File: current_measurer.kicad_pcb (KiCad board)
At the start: 2 copper layers, 104.9 x 128.5 mm, 31 parts, among them J1 Eurorack Power Input, J2 Eurorack Power Output, J3 Back_Conn_2, J4 Front_Conn_2, J5 Back_Conn_3, J6 Front_Conn_3, J7 Back_Conn_1, J8 Front_Conn_1, M2 MountingHole_2.2mm_M2, M3 MountingHole_3.2mm_M3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

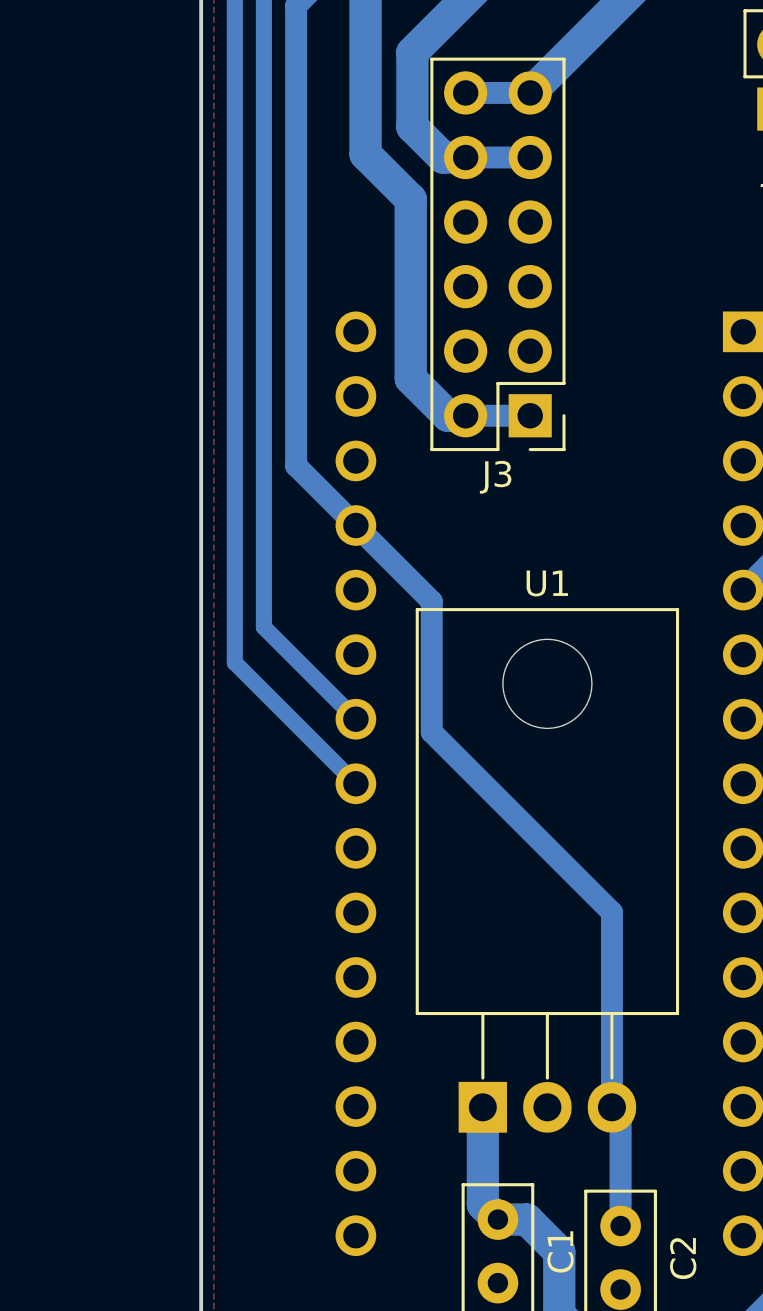
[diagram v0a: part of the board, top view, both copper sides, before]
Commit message: Add extra pin for VIN
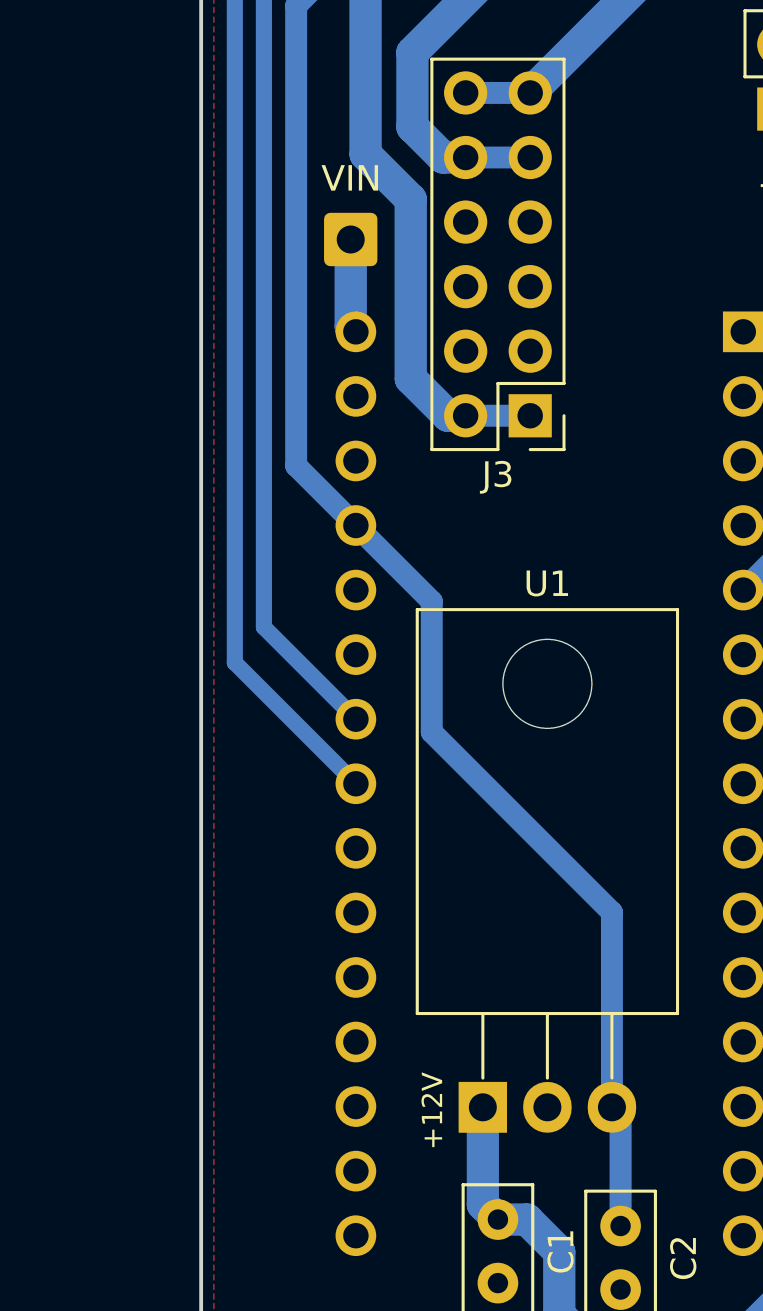
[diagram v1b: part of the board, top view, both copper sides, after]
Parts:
- added J9: VIN, Connector_Wire:SolderWire-0.5sqmm_1x01_D0.9mm_OD2.1mm, F.Cu at (122.9, 96.6)
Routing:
- net Net-(A1-Pad30): track 0.00 -> 3.72 mm
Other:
- board text added: "+12V"
- board text added: "VIN"

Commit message: Tweak final things before making gerbers for 1.2
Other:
- rule pad_to_mask_clearance: 0.0508 -> 0.1

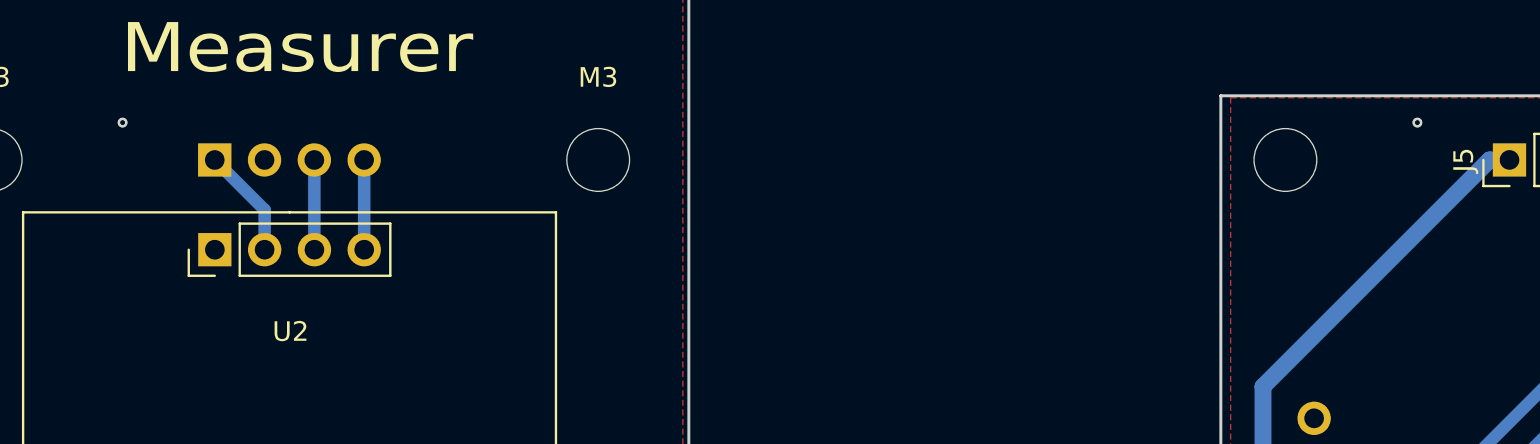
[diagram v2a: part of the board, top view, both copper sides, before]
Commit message: Update project to Kicad 6+ format
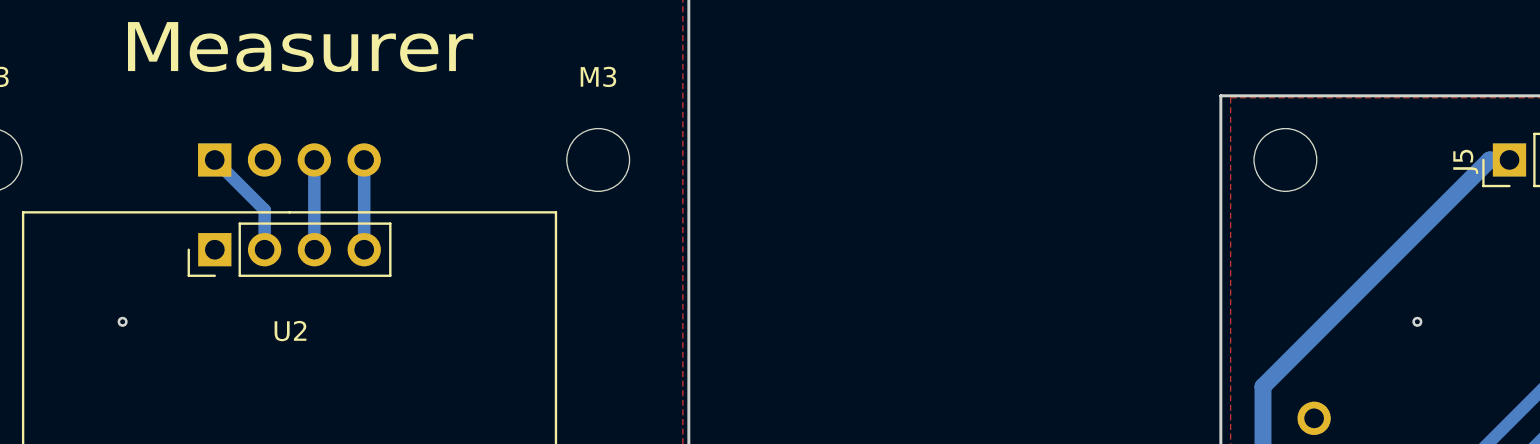
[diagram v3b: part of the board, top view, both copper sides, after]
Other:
- board text added: "MAIN BOARD V1.3 -- 2021/12/05"
- board text added: "PANEL V1.3 -- 2021/12/05"
- board text added: "USB END"
- board text removed: "MAIN BOARD V1.2 -- 2021/11/13"
- board text removed: "PANEL V1.2 -- 2021/11/13"
